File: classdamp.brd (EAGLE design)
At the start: 88.6 x 36.8 mm, 40 parts, among them Q1 BS170, Q2 BS170

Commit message: Adjusting...
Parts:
- moved H1 1.21 mm to (4.45, 34.1)
- moved H2 1.03 mm to (84.5, 34.1)
- moved H4 0.68 mm to (4.45, 4.04)
- moved H3 0.23 mm to (84.5, 4.04)
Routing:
- net N$8: track 7.78 -> 7.03 mm
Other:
- board size 88.6 x 36.8 mm -> 88.6 x 38.1 mm
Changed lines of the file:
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@@
 <setting verticaltext="up"/>
 </settings>
-<grid distance="0.05" unitdist="inch" unit="mm" style="lines" multiple="1" display="no" altdistance="0.025" altunitdist="inch" altunit="inch"/>
+<grid distance="0.05" unitdist="inch" unit="inch" style="lines" multiple="1" display="no" altdistance="0.025" altunitdist="inch" altunit="inch"/>
 <layers>
 <layer number="1" name="Top" color="4" fill="1" visible="yes" active="yes"/>
@@
 <plain>
 <wire x1="0" y1="0" x2="88.57" y2="0" width="0" layer="20"/>
-<wire x1="88.57" y1="0" x2="88.57" y2="36.82" width="0" layer="20"/>
-<wire x1="88.57" y1="36.82" x2="0" y2="36.82" width="0" layer="20"/>
-<wire x1="0" y1="36.82" x2="0" y2="0" width="0" layer="20"/>
+<wire x1="88.57" y1="0" x2="88.57" y2="38.09" width="0" layer="20"/>
+<wire x1="88.57" y1="38.09" x2="0" y2="38.09" width="0" layer="20"/>
+<wire x1="0" y1="38.09" x2="0" y2="0" width="0" layer="20"/>
 <text x="86.995" y="19.05" size="1.778" layer="16" font="vector" ratio="14" rot="MR270">D-Amp</text>
 <text x="4.445" y="30.48" size="1.778" layer="16" font="vector" ratio="15" rot="MR270">Signal Generator</text>
-<dimension x1="0" y1="38.1" x2="88.9" y2="38.1" x3="44.45" y3="43.18" textsize="1.778" textratio="15" layer="47"/>
-<dimension x1="89.84" y1="0" x2="89.84" y2="36.82" x3="96.52" y3="18.41" textsize="1.778" textratio="15" layer="47"/>
-<dimension x1="84.455" y1="33.02" x2="84.455" y2="3.81" x3="92.71" y3="18.415" textsize="1.778" textratio="15" layer="47"/>
-<dimension x1="3.81" y1="33.02" x2="84.455" y2="33.02" x3="44.1325" y3="39.37" textsize="1.778" textratio="15" layer="47"/>
+<dimension x1="0" y1="39.37" x2="88.9" y2="39.37" x3="44.45" y3="44.45" textsize="1.778" textratio="15" layer="47"/>
+<dimension x1="89.84" y1="0" x2="89.84" y2="38.09" x3="96.52" y3="19.045" textsize="1.778" textratio="15" layer="47" precision="1"/>
+<dimension x1="84.455" y1="33.655" x2="4.445" y2="33.655" x3="44.45" y3="40.64" textsize="1.778" textratio="15" layer="47"/>
+<dimension x1="84.455" y1="4.045" x2="84.455" y2="34.055" x3="92.71" y3="19.05" textsize="1.778" textratio="15" layer="47"/>
 </plain>
 <attributes>
@@
 <attribute name="OC_FARNELL" value="unknown" x="77.47" y="12.7" size="1.778" layer="27" rot="R270" display="off"/>
 </element>
-<element name="H2" library="holes" package="3,2" value="MOUNT-HOLE3.2" x="84.455" y="33.02" rot="MR0"/>
-<element name="H3" library="holes" package="3,2" value="MOUNT-HOLE3.2" x="84.455" y="3.81"/>
-<element name="H4" library="holes" package="3,2" value="MOUNT-HOLE3.2" x="3.81" y="3.81"/>
-<element name="H1" library="holes" package="3,2" value="MOUNT-HOLE3.2" x="3.81" y="33.02"/>
+<element name="H2" library="holes" package="3,2" value="MOUNT-HOLE3.2" x="84.455" y="34.055" rot="MR0"/>
+<element name="H3" library="holes" package="3,2" value="MOUNT-HOLE3.2" x="84.455" y="4.045"/>
+<element name="H4" library="holes" package="3,2" value="MOUNT-HOLE3.2" x="4.445" y="4.045"/>
+<element name="H1" library="holes" package="3,2" value="MOUNT-HOLE3.2" x="4.445" y="34.055"/>
 <element name="JP2" library="pinhead" package="1X03" value="ISP1" x="38.1" y="10.16" rot="R90"/>
 <element name="JP8" library="pinhead" package="1X03" value="ISP2" x="38.1" y="27.94" rot="R270"/>
@@
 <contactref element="JP4" pad="1"/>
 <contactref element="C6" pad="-"/>
-<wire x1="15.621" y1="7.62" x2="15.621" y2="11.049" width="0.6096" layer="16"/>
-<wire x1="15.621" y1="11.049" x2="15.24" y2="11.43" width="0.6096" layer="16"/>
-<wire x1="15.24" y1="11.43" x2="11.43" y2="11.43" width="0.6096" layer="16"/>
+<wire x1="15.621" y1="7.62" x2="15.621" y2="9.779" width="0.6096" layer="16"/>
+<wire x1="15.621" y1="9.779" x2="13.97" y2="11.43" width="0.6096" layer="16"/>
+<wire x1="13.97" y1="11.43" x2="11.43" y2="11.43" width="0.6096" layer="16"/>
 </signal>
 <signal name="N$10">

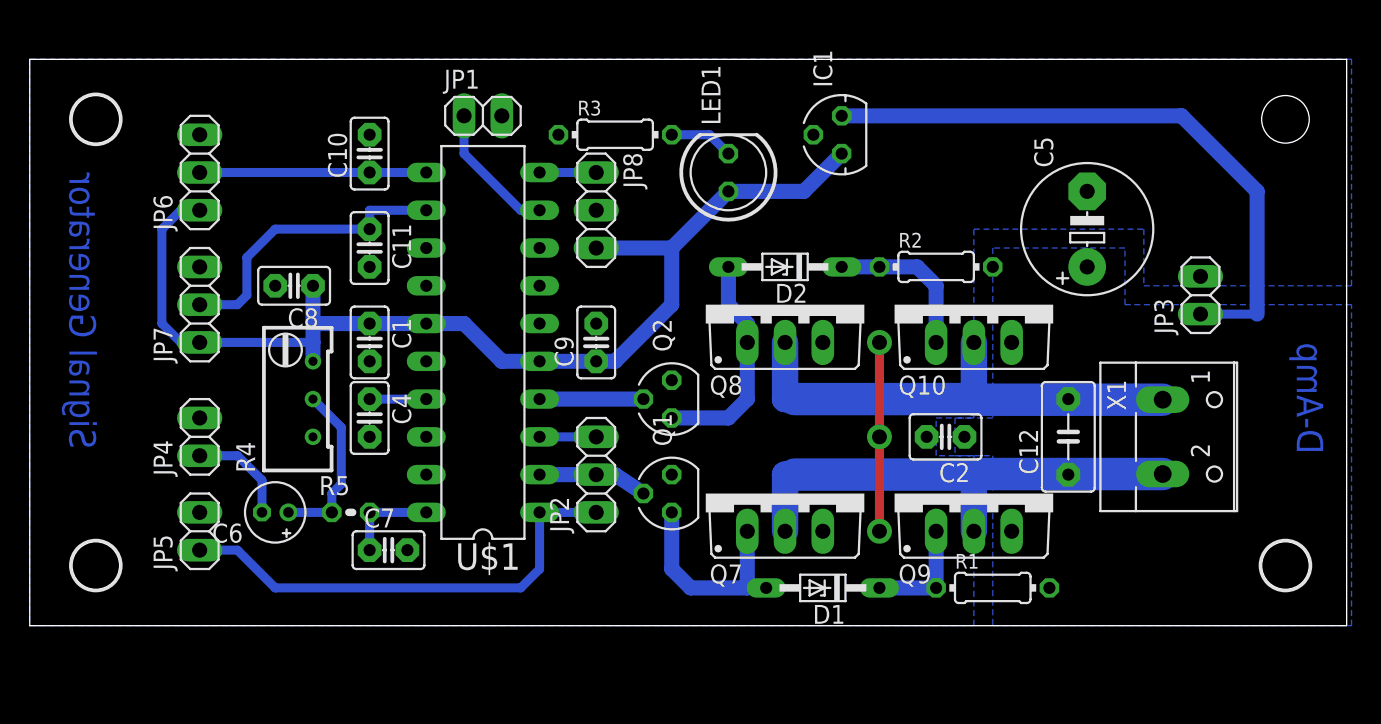
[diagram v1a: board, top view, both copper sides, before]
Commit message: R/C durch SMD ersetzt - bessere GND-Flächen
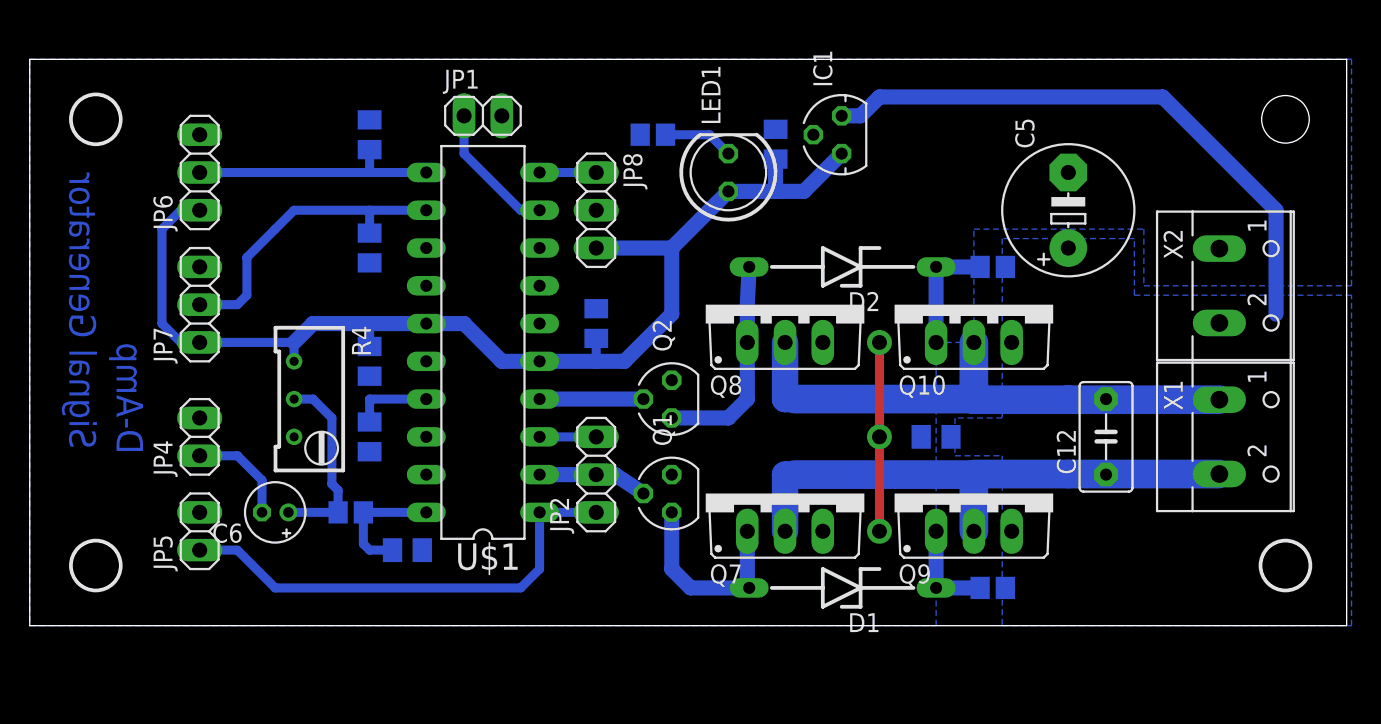
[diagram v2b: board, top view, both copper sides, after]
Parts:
- removed C10, C11: 100n, capacitor-wima:C2.5-2
- removed JP3: (no value), pinhead:1X02
- added C13, C3: 100n, resistor:C0805K
- added X2: (no value), con-wago-500:W237-102
- C1, C4, C7, C8, C9: device capacitor-wima:C2.5-2 -> resistor:C0805K
- C2: device capacitor-wima:C2.5-3 -> resistor:C0805K
- D1, D2: device diode:DO34Z7 -> diode:ZDIO12.5
- R1, R2: device resistor:0204/7 -> resistor:R0805
- R3: value (none) -> 1k; device resistor:0204/7 -> resistor:R0805
- R5: device resistor:0204V -> resistor:R0805
- moved C1 30.4 mm to (50.2, 32.4), flipped to the bottom, turned to 90 degrees
- moved C9 16.5 mm to (22.9, 25.4), flipped to the bottom, turned to 270 degrees
- moved C8 11.4 mm to (22.9, 33.0), flipped to the bottom, turned to 90 degrees
- moved D2 3.81 mm to (54.6, 24.1)
- moved X1 3.81 mm to (81.3, 12.7)
- moved R2 3.81 mm to (64.8, 24.1), flipped to the bottom, turned to 180 degrees
- moved C12 2.54 mm to (72.4, 12.7)
- moved R3 2.54 mm to (41.9, 33.0), flipped to the bottom, turned to 180 degrees
- moved C5 1.80 mm to (69.8, 27.9)
- moved C4 1.27 mm to (22.9, 12.7), flipped to the bottom
- moved C7 1.27 mm to (25.4, 5.08), flipped to the bottom, turned to 180 degrees
- moved R4 1.27 mm to (19.1, 15.2), turned to 180 degrees
- moved D1 1.27 mm to (54.6, 2.54)
- moved C2 0.63 mm to (61.0, 12.7), flipped to the bottom, turned to 0 degrees
- flipped R1 to the bottom, turned to 180 degrees
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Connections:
- net +12V: now also X2.2; no longer JP3.1
- net +5V: now also C13.1, C3.1, R4.1; no longer C8.1, C9.1, R4.3
- net ADC1: now also R5.1; no longer R5.2
- net ADC2: now also C8.1; no longer C10.1
- net ADC3: now also C9.1; no longer C11.1
- net GND: now also C13.2, C3.2, R4.3, X2.1; no longer C10.2, C11.2, JP3.2, R4.1
- net N$10: now also R5.2; no longer R5.1
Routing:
- net N$13: track 33.1 -> 39.4 mm
- net N$11: track 33.1 -> 39.4 mm
- net N$7: track 10.7 -> 8.04 mm
- net +5V: track 74.9 -> 77.2 mm
- net +12V: track 42.1 -> 39.9 mm
- net ADC1: track 6.35 -> 8.48 mm
- net ADC2: track 15.2 -> 16.8 mm
- net N$2: track 3.81 -> 5.35 mm
- net N$10: track 11.6 -> 12.9 mm
- net N$4: track 14.5 -> 13.4 mm
- net N$6: track 7.62 -> 6.77 mm
- net ADC3: track 20.1 -> 20.9 mm
- net N$5: track 15.0 -> 14.5 mm

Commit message: few details
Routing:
- net ADC3: track 20.9 -> 21.6 mm
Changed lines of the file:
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@@
 <contactref element="Q10" pad="S"/>
 <polygon width="0.254" layer="16" isolate="0.4064">
-<vertex x="65.405" y="26.035"/>
+<vertex x="65.405" y="25.7175"/>
 <vertex x="65.405" y="13.97"/>
 <vertex x="62.23" y="13.97"/>
@@
 <vertex x="65.405" y="11.43"/>
 <vertex x="65.405" y="0"/>
-<vertex x="88.9" y="0"/>
-<vertex x="88.9" y="22.225"/>
-<vertex x="74.295" y="22.225"/>
-<vertex x="74.295" y="26.035"/>
+<vertex x="88.265" y="0"/>
+<vertex x="88.265" y="21.9075"/>
+<vertex x="73.9775" y="21.9075"/>
+<vertex x="73.9775" y="25.7175"/>
 </polygon>
 <wire x1="76.2" y1="35.56" x2="83.82" y2="27.94" width="1.016" layer="16"/>
@@
 <contactref element="U$1" pad="12"/>
 <wire x1="26.67" y1="27.94" x2="22.86" y2="27.94" width="0.6096" layer="16"/>
-<wire x1="11.43" y1="21.59" x2="13.97" y2="21.59" width="0.6096" layer="16"/>
-<wire x1="13.97" y1="21.59" x2="14.605" y2="22.225" width="0.6096" layer="16"/>
-<wire x1="14.605" y1="22.225" x2="14.605" y2="24.765" width="0.6096" layer="16"/>
-<wire x1="14.605" y1="24.765" x2="16.51" y2="26.67" width="0.6096" layer="16"/>
+<wire x1="11.43" y1="21.59" x2="17.78" y2="21.59" width="0.6096" layer="16"/>
+<wire x1="17.78" y1="21.59" x2="19.05" y2="22.86" width="0.6096" layer="16"/>
+<wire x1="19.05" y1="22.86" x2="19.05" y2="26.67" width="0.6096" layer="16"/>
+<wire x1="19.05" y1="26.67" x2="20.32" y2="27.94" width="0.6096" layer="16"/>
 <contactref element="C9" pad="1"/>
-<wire x1="22.86" y1="27.94" x2="17.78" y2="27.94" width="0.6096" layer="16"/>
-<wire x1="17.78" y1="27.94" x2="16.51" y2="26.67" width="0.6096" layer="16"/>
+<wire x1="22.86" y1="27.94" x2="20.32" y2="27.94" width="0.6096" layer="16"/>
 <wire x1="22.86" y1="27.94" x2="22.86" y2="26.4" width="0.6096" layer="16"/>
 </signal>

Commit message: added partlist
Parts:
- IC1: value (none) -> 78L05
- Q10, Q9: value (none) -> IRF 9Z34N
- Q7, Q8: value (none) -> IRF 530N
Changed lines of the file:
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@@
 </autorouter>
 <elements>
-<element name="IC1" library="v-reg" package="78LXX" value="" x="54.61" y="33.02" rot="R90"/>
+<element name="IC1" library="v-reg" package="78LXX" value="78L05" x="54.61" y="33.02" rot="R90"/>
 <element name="D1" library="diode" package="ZDIO12.5" value="6.3V" x="54.61" y="2.54" rot="R180"/>
 <element name="Q1" library="transistor-small-signal" package="SOT54E" value="BS170" x="43.18" y="8.89" rot="R90"/>
@@
 <element name="C6" library="resistor" package="E1,8-4" value="10uF" x="16.51" y="7.62" rot="R180"/>
 <element name="U$1" library="avr-7" package="DIL20" value="TINY26P" x="30.48" y="19.05" rot="R90"/>
-<element name="Q7" library="transistor-power" package="TO220BV" value="" x="50.8" y="8.89"/>
-<element name="Q8" library="transistor-power" package="TO220BV" value="" x="50.8" y="21.59"/>
-<element name="Q9" library="transistor-power" package="TO220BV" value="" x="63.5" y="8.89"/>
-<element name="Q10" library="transistor-power" package="TO220BV" value="" x="63.5" y="21.59"/>
+<element name="Q7" library="transistor-power" package="TO220BV" value="IRF 530N" x="50.8" y="8.89"/>
+<element name="Q8" library="transistor-power" package="TO220BV" value="IRF 530N" x="50.8" y="21.59"/>
+<element name="Q9" library="transistor-power" package="TO220BV" value="IRF 9Z34N" x="63.5" y="8.89"/>
+<element name="Q10" library="transistor-power" package="TO220BV" value="IRF 9Z34N" x="63.5" y="21.59"/>
 <element name="JP5" library="pinhead" package="1X02" value="Inp_Sel" x="11.43" y="6.35" rot="R90"/>
 <element name="X1" library="con-wago-500" package="W237-102" value="" x="81.28" y="12.7" rot="R270">

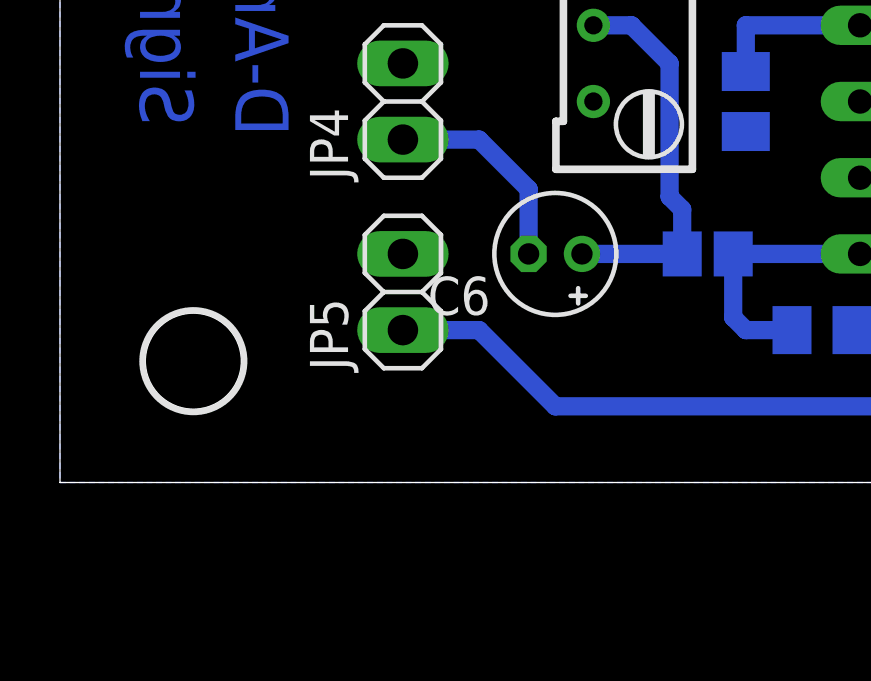
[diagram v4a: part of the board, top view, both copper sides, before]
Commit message: updated reichelt order
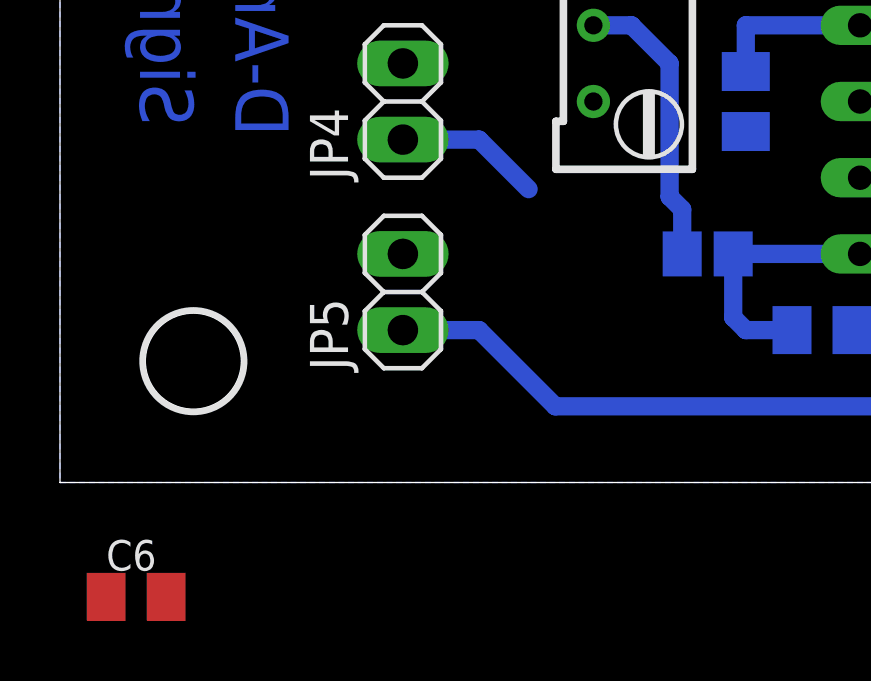
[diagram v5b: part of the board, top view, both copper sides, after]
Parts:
- C6: value 10uF -> 10u; device resistor:E1,8-4 -> resistor:C0805K
- moved C6 18.1 mm to (2.54, -3.81), turned to 0 degrees
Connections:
- net N$10: now also C6.1; no longer C6.+
- net N$8: now also C6.2; no longer C6.-
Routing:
- net N$10: track 12.9 -> 9.59 mm
- net N$8: track 7.03 -> 4.87 mm
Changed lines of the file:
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@@
 <element name="JP6" library="pinhead" package="1X03" value="freq_pot" x="11.43" y="30.48" rot="R90"/>
 <element name="JP7" library="pinhead" package="1X03" value="vol_pot" x="11.43" y="21.59" rot="R90"/>
-<element name="C6" library="resistor" package="E1,8-4" value="10uF" x="16.51" y="7.62" rot="R180"/>
 <element name="U$1" library="avr-7" package="DIL20" value="TINY26P" x="30.48" y="19.05" rot="R90"/>
 <element name="Q7" library="transistor-power" package="TO220BV" value="IRF 530N" x="50.8" y="8.89"/>
@@
 <element name="C7" library="resistor" package="C0805K" value="1n" x="25.4" y="5.08" rot="MR180"/>
 <element name="R5" library="resistor" package="R0805" value="10k" x="21.59" y="7.62" rot="MR0"/>
+<element name="C6" library="resistor" package="C0805K" value="10u" x="2.54" y="-3.81"/>
 </elements>
 <signals>
@@
 <signal name="N$8">
 <contactref element="JP4" pad="1"/>
-<contactref element="C6" pad="-"/>
-<wire x1="15.621" y1="7.62" x2="15.621" y2="9.779" width="0.6096" layer="16"/>
 <wire x1="15.621" y1="9.779" x2="13.97" y2="11.43" width="0.6096" layer="16"/>
 <wire x1="13.97" y1="11.43" x2="11.43" y2="11.43" width="0.6096" layer="16"/>
+<contactref element="C6" pad="2"/>
+<wire x1="3.54" y1="-3.81" x2="11.43" y2="11.43" width="0" layer="19" extent="1-1"/>
 </signal>
 <signal name="N$10">
-<contactref element="C6" pad="+"/>
 <contactref element="R4" pad="2"/>
 <wire x1="17.78" y1="15.24" x2="19.05" y2="15.24" width="0.6096" layer="16"/>
 <contactref element="R5" pad="2"/>
-<wire x1="17.399" y1="7.62" x2="20.74" y2="7.62" width="0.6096" layer="16"/>
 <wire x1="20.74" y1="7.62" x2="20.74" y2="9.105" width="0.6096" layer="16"/>
 <wire x1="20.74" y1="9.105" x2="20.32" y2="9.525" width="0.6096" layer="16"/>
 <wire x1="19.05" y1="15.24" x2="20.32" y2="13.97" width="0.6096" layer="16"/>
 <wire x1="20.32" y1="13.97" x2="20.32" y2="9.525" width="0.6096" layer="16"/>
+<contactref element="C6" pad="1"/>
+<wire x1="1.54" y1="-3.81" x2="20.74" y2="7.62" width="0" layer="19" extent="1-16"/>
 </signal>
 <signal name="ADC1">

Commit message: few changes
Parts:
- moved C6 18.1 mm to (16.5, 7.62), flipped to the bottom
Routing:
- net N$10: track 9.59 -> 12.8 mm
- net N$8: track 4.87 -> 7.14 mm
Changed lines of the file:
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@@
 <element name="C7" library="resistor" package="C0805K" value="1n" x="25.4" y="5.08" rot="MR180"/>
 <element name="R5" library="resistor" package="R0805" value="10k" x="21.59" y="7.62" rot="MR0"/>
-<element name="C6" library="resistor" package="C0805K" value="10u" x="2.54" y="-3.81"/>
+<element name="C6" library="resistor" package="C0805K" value="10u" x="16.51" y="7.62" rot="MR0"/>
 </elements>
 <signals>
@@
 <wire x1="13.97" y1="11.43" x2="11.43" y2="11.43" width="0.6096" layer="16"/>
 <contactref element="C6" pad="2"/>
-<wire x1="3.54" y1="-3.81" x2="11.43" y2="11.43" width="0" layer="19" extent="1-1"/>
+<wire x1="15.51" y1="7.62" x2="15.621" y2="7.62" width="0.6096" layer="16"/>
+<wire x1="15.621" y1="7.62" x2="15.621" y2="9.779" width="0.6096" layer="16"/>
 </signal>
 <signal name="N$10">
@@
 <wire x1="20.32" y1="13.97" x2="20.32" y2="9.525" width="0.6096" layer="16"/>
 <contactref element="C6" pad="1"/>
-<wire x1="1.54" y1="-3.81" x2="20.74" y2="7.62" width="0" layer="19" extent="1-16"/>
+<wire x1="17.51" y1="7.62" x2="20.74" y2="7.62" width="0.6096" layer="16"/>
 </signal>
 <signal name="ADC1">
